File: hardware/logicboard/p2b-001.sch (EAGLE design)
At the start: 54 parts, among them IC1 74LS06N, IC2 4066N, J1 MKR, J2 GPIO, J3 Vcc, J4 RLY, J5 SPI, J7 DIN5, J8 DIN5, J9 DIN5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

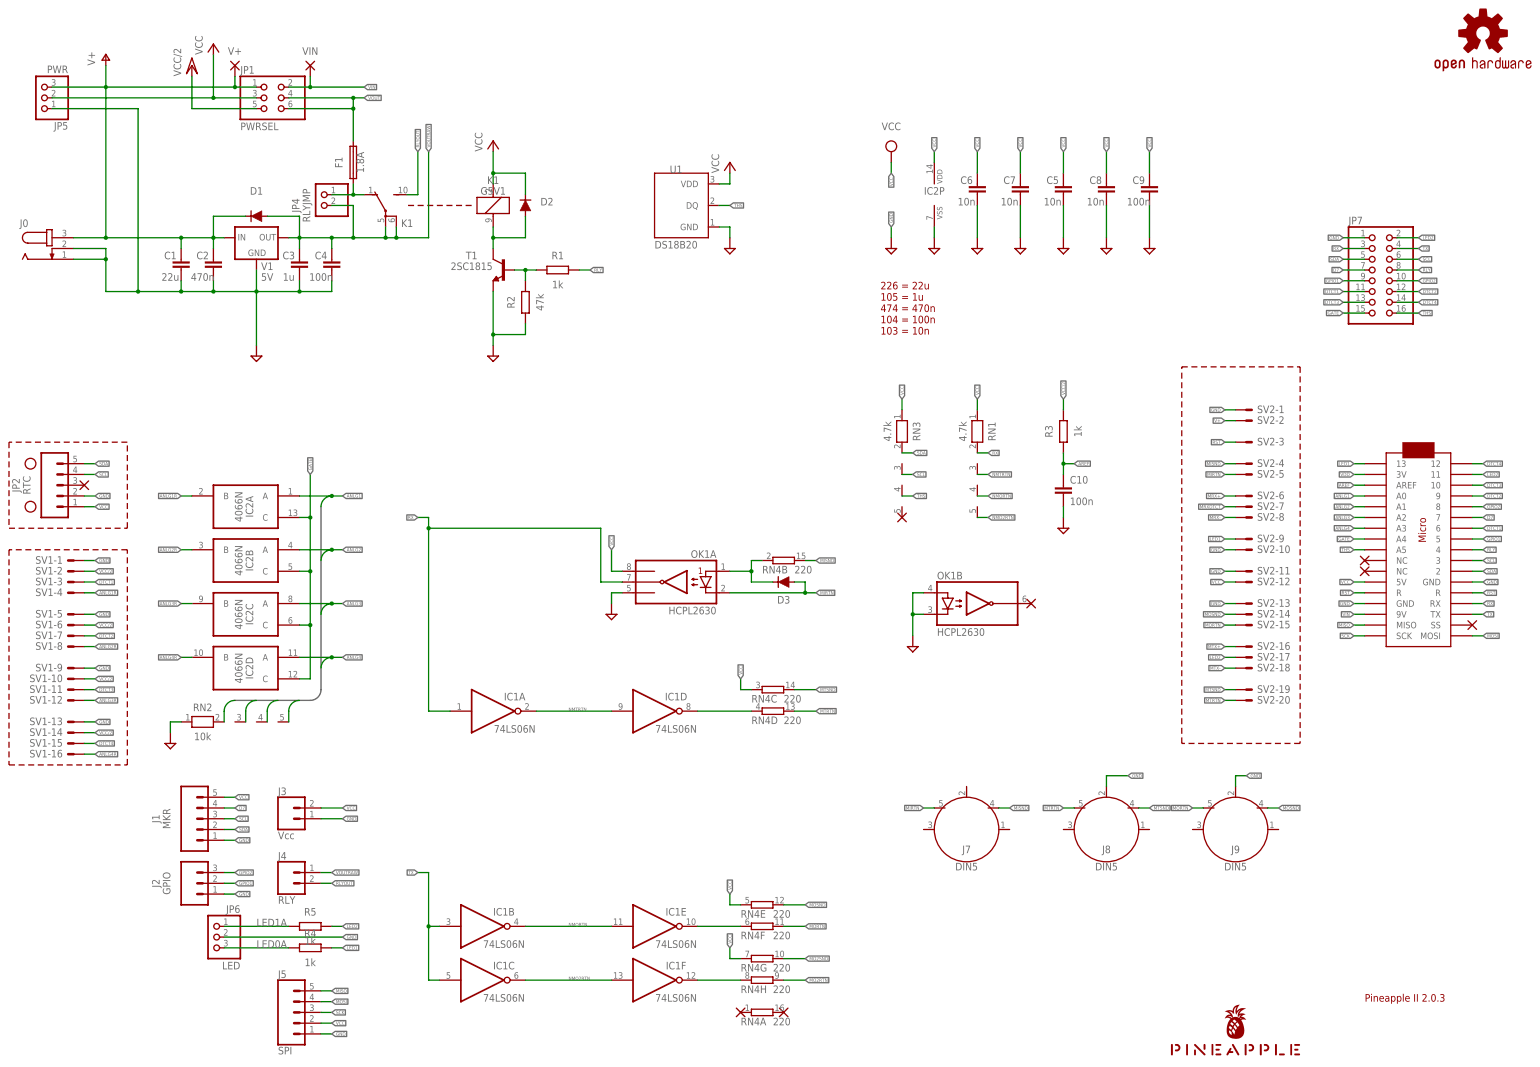
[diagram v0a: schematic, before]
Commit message: Followed Pineapple II 2.4.0 design. Before autorouting.
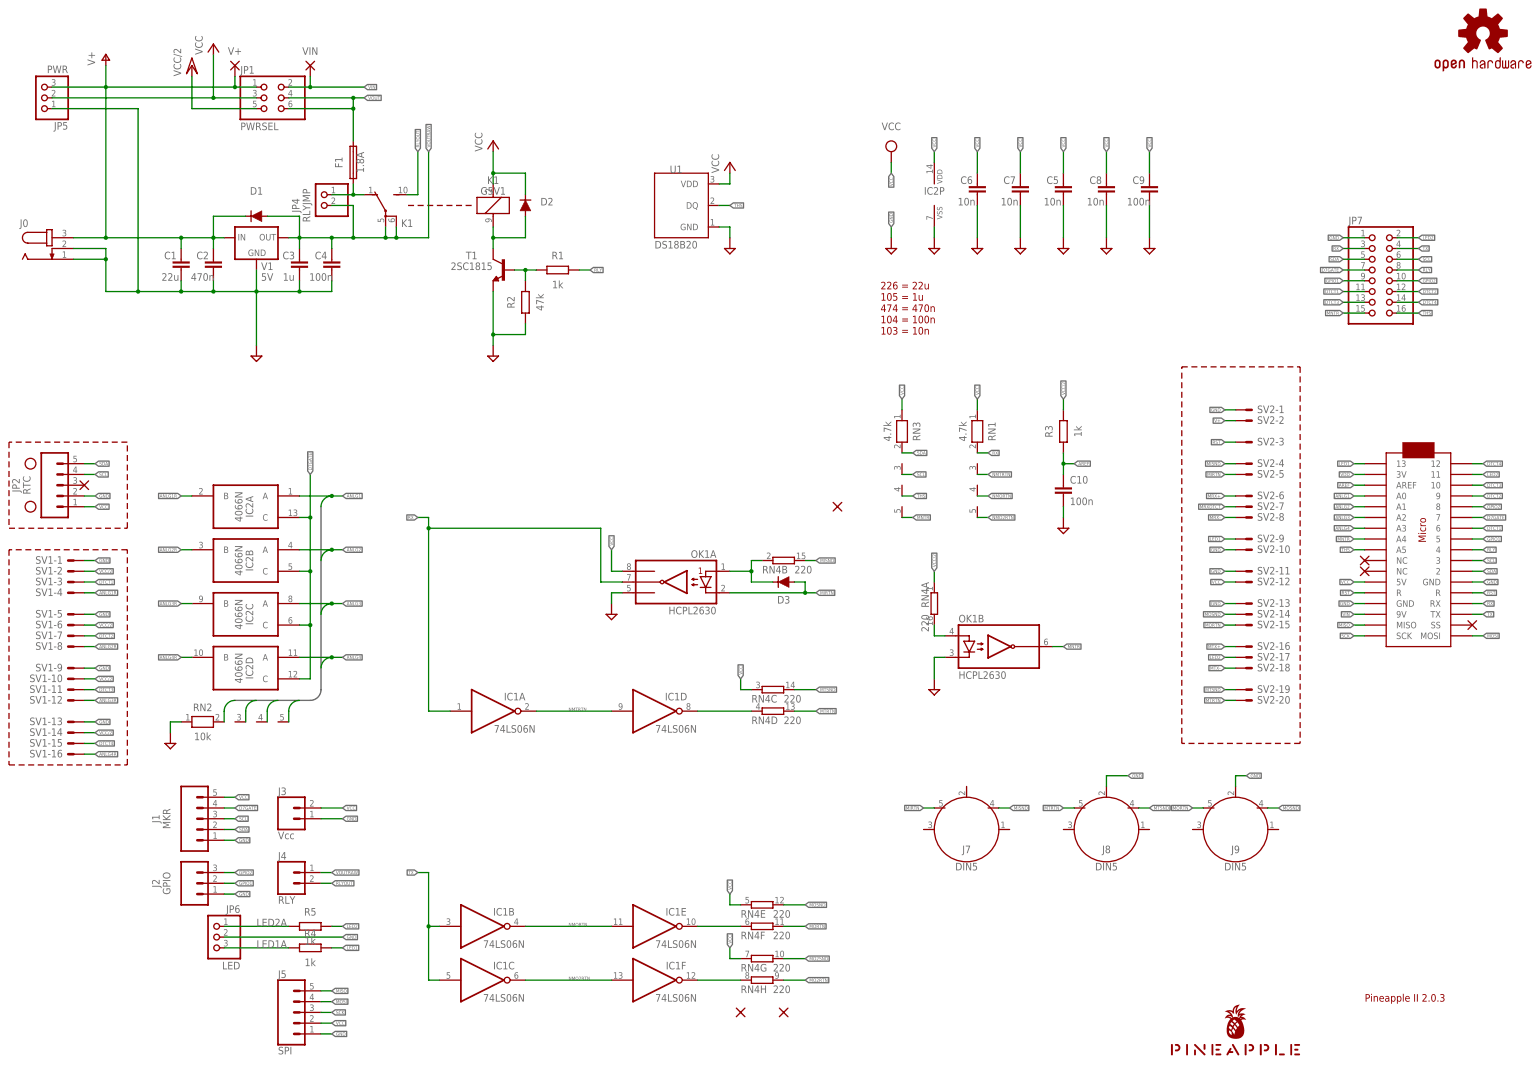
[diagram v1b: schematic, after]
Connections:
- removed net D7: J1.4, JP7.7, MC1.7
- removed net GATE: IC2A.C, IC2B.C, IC2C.C, IC2D.C, JP7.15, MC1.A4
- removed net LED0A: JP6.3, R4.1
- new net D7GATE: IC2A.C, IC2B.C, IC2C.C, IC2D.C, J1.4, JP7.7, MC1.7
- new net LED2A: JP6.1, R5.1
- new net MNTR: JP7.15, MC1.A4, OK1B.VO2, RN3.5
- new net MNTRA: OK1B.A2, RN4A.2
- net GND: no longer OK1B.A2
- net LED1A: now also JP6.3, R4.1; no longer JP6.1, R5.1
- net VCC/2: now also RN4A.1
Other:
- moved on the sheet: OK1B, RN4A
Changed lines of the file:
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@@
 <part name="OK1" library="optocoupler" library_urn="urn:adsk.eagle:library:320" deviceset="HCPL2630" device="" package3d_urn="urn:adsk.eagle:package:21941/1"/>
 <part name="SUPPLY1" library="supply2" deviceset="GND" device=""/>
-<part name="X2" library="wirepad" library_urn="urn:adsk.eagle:library:412" deviceset="PAD-N" device=""/>
 <part name="V+" library="wirepad" library_urn="urn:adsk.eagle:library:412" deviceset="SMD2" device="" package3d_urn="urn:adsk.eagle:package:30839/1"/>
 <part name="VIN" library="wirepad" library_urn="urn:adsk.eagle:library:412" deviceset="SMD2" device="" package3d_urn="urn:adsk.eagle:package:30839/1"/>
@@
 <attribute name="NAME" x="86.36" y="25.908" size="1.778" layer="95" font="vector"/>
 </instance>
-<instance part="RN4" gate="A" x="200.66" y="17.78" smashed="yes">
-<attribute name="VALUE" x="203.2" y="14.732" size="1.778" layer="96"/>
-<attribute name="NAME" x="195.58" y="14.732" size="1.778" layer="95"/>
+<instance part="RN4" gate="A" x="241.3" y="114.3" smashed="yes" rot="R270">
+<attribute name="VALUE" x="238.252" y="111.76" size="1.778" layer="96" rot="R270"/>
+<attribute name="NAME" x="238.252" y="119.38" size="1.778" layer="95" rot="R270"/>
 </instance>
 <instance part="RN4" gate="B" x="205.74" y="124.46" smashed="yes">
@@
 <attribute name="VALUE" x="231.14" y="154.94" size="1.778" layer="96" rot="R270" align="top-center"/>
 </instance>
-<instance part="X101" gate="G$1" x="233.68" y="134.62" smashed="yes"/>
+<instance part="X101" gate="G$1" x="218.44" y="137.16" smashed="yes"/>
 <instance part="OK1" gate="A" x="180.34" y="119.38" smashed="yes" rot="MR0">
 <attribute name="NAME" x="189.865" y="125.095" size="1.778" layer="95" rot="MR0"/>
 <attribute name="VALUE" x="189.865" y="111.76" size="1.778" layer="96" rot="MR0"/>
 </instance>
-<instance part="OK1" gate="B" x="251.46" y="114.3" smashed="yes">
-<attribute name="NAME" x="241.935" y="120.015" size="1.778" layer="95"/>
-<attribute name="VALUE" x="241.935" y="106.68" size="1.778" layer="96"/>
-</instance>
-<instance part="SUPPLY1" gate="GND" x="236.22" y="104.14" smashed="yes"/>
-<instance part="X2" gate="G$1" x="264.16" y="114.3" smashed="yes"/>
+<instance part="OK1" gate="B" x="256.54" y="104.14" smashed="yes">
+<attribute name="NAME" x="247.015" y="109.855" size="1.778" layer="95"/>
+<attribute name="VALUE" x="247.015" y="96.52" size="1.778" layer="96"/>
+</instance>
+<instance part="SUPPLY1" gate="GND" x="241.3" y="93.98" smashed="yes"/>
 <instance part="V+" gate="1" x="76.2" y="241.3" smashed="yes" rot="R270">
 <attribute name="NAME" x="76.2" y="243.84" size="1.778" layer="95" align="bottom-center"/>
@@
 </segment>
 <segment>
-<pinref part="OK1" gate="B" pin="A2"/>
-<wire x1="238.76" y1="116.84" x2="236.22" y2="116.84" width="0.1524" layer="91"/>
 <pinref part="OK1" gate="B" pin="C2"/>
-<wire x1="238.76" y1="111.76" x2="236.22" y2="111.76" width="0.1524" layer="91"/>
-<wire x1="236.22" y1="111.76" x2="236.22" y2="116.84" width="0.1524" layer="91"/>
-<wire x1="236.22" y1="111.76" x2="236.22" y2="106.68" width="0.1524" layer="91"/>
-<junction x="236.22" y="111.76"/>
+<wire x1="243.84" y1="101.6" x2="241.3" y2="101.6" width="0.1524" layer="91"/>
+<wire x1="241.3" y1="101.6" x2="241.3" y2="96.52" width="0.1524" layer="91"/>
 <pinref part="SUPPLY1" gate="GND" pin="GND"/>
 </segment>
@@
 </segment>
 </net>
-<net name="GATE" class="0">
+<net name="MNTR" class="0">
 <segment>
 <pinref part="MC1" gate="G$1" pin="A4"/>
 <wire x1="342.9" y1="129.54" x2="340.36" y2="129.54" width="0.1524" layer="91"/>
 <label x="340.36" y="129.54" size="0.8128" layer="95" rot="MR0" xref="yes"/>
+</segment>
+<segment>
+<pinref part="JP7" gate="A" pin="15"/>
+<wire x1="342.9" y1="182.88" x2="337.82" y2="182.88" width="0.1524" layer="91"/>
+<label x="337.82" y="182.88" size="0.8128" layer="95" rot="R180" xref="yes"/>
+</segment>
+<segment>
+<pinref part="RN3" gate="1" pin="5"/>
+<wire x1="233.68" y1="134.62" x2="236.22" y2="134.62" width="0.1524" layer="91"/>
+<label x="236.22" y="134.62" size="0.8128" layer="95" xref="yes"/>
+</segment>
+<segment>
+<pinref part="OK1" gate="B" pin="VO2"/>
+<wire x1="269.24" y1="104.14" x2="271.78" y2="104.14" width="0.1524" layer="91"/>
+<label x="271.78" y="104.14" size="0.8128" layer="95" xref="yes"/>
+</segment>
+</net>
+<net name="VDD" class="2">
+<segment>
+<pinref part="MC1" gate="G$1" pin="3V"/>
+<wire x1="342.9" y1="144.78" x2="340.36" y2="144.78" width="0.1524" layer="91"/>
+<label x="340.36" y="144.78" size="0.8128" layer="95" rot="MR0" xref="yes"/>
+</segment>
+</net>
+<net name="LED2" class="0">
+<segment>
+<pinref part="MC1" gate="G$1" pin="11"/>
+<wire x1="368.3" y1="144.78" x2="370.84" y2="144.78" width="0.1524" layer="91"/>
+<label x="370.84" y="144.78" size="0.8128" layer="95" xref="yes"/>
+</segment>
+<segment>
+<wire x1="99.06" y1="38.1" x2="101.6" y2="38.1" width="0.1524" layer="91"/>
+<label x="101.6" y="38.1" size="0.8128" layer="95" xref="yes"/>
+<pinref part="R5" gate="G$1" pin="2"/>
+</segment>
+<segment>
+<pinref part="JP7" gate="A" pin="2"/>
+<wire x1="350.52" y1="200.66" x2="355.6" y2="200.66" width="0.1524" layer="91"/>
+<label x="355.6" y="200.66" size="0.8128" layer="95" xref="yes"/>
+</segment>
+<segment>
+<pinref part="SV2" gate="-17" pin="S"/>
+<wire x1="312.42" y1="101.6" x2="309.88" y2="101.6" width="0.1524" layer="91"/>
+<label x="309.88" y="101.6" size="0.8128" layer="95" rot="MR0" xref="yes"/>
+</segment>
+</net>
+<net name="MRX-" class="0">
+<segment>
+<pinref part="SV2" gate="-8" pin="S"/>
+<wire x1="312.42" y1="134.62" x2="309.88" y2="134.62" width="0.1524" layer="91"/>
+<label x="309.88" y="134.62" size="0.8128" layer="95" rot="MR0" xref="yes"/>
+</segment>
+</net>
+<net name="D7GATE" class="0">
+<segment>
+<pinref part="MC1" gate="G$1" pin="7"/>
+<wire x1="368.3" y1="134.62" x2="370.84" y2="134.62" width="0.1524" layer="91"/>
+<label x="370.84" y="134.62" size="0.8128" layer="95" xref="yes"/>
+</segment>
+<segment>
+<pinref part="J1" gate="G$1" pin="4"/>
+<wire x1="73.66" y1="66.04" x2="76.2" y2="66.04" width="0.1524" layer="91"/>
+<label x="76.2" y="66.04" size="0.8128" layer="95" xref="yes"/>
+</segment>
+<segment>
+<pinref part="JP7" gate="A" pin="7"/>
+<wire x1="342.9" y1="193.04" x2="337.82" y2="193.04" width="0.1524" layer="91"/>
+<label x="337.82" y="193.04" size="0.8128" layer="95" rot="R180" xref="yes"/>
 </segment>
 <segment>
@@
 <label x="93.98" y="144.78" size="0.8128" layer="95" rot="R90" xref="yes"/>
 </segment>
-<segment>
-<pinref part="JP7" gate="A" pin="15"/>
-<wire x1="342.9" y1="182.88" x2="337.82" y2="182.88" width="0.1524" layer="91"/>
-<label x="337.82" y="182.88" size="0.8128" layer="95" rot="R180" xref="yes"/>
-</segment>
-</net>
-<net name="VDD" class="2">
-<segment>
-<pinref part="MC1" gate="G$1" pin="3V"/>
-<wire x1="342.9" y1="144.78" x2="340.36" y2="144.78" width="0.1524" layer="91"/>
-<label x="340.36" y="144.78" size="0.8128" layer="95" rot="MR0" xref="yes"/>
-</segment>
-</net>
-<net name="LED2" class="0">
-<segment>
-<pinref part="MC1" gate="G$1" pin="11"/>
-<wire x1="368.3" y1="144.78" x2="370.84" y2="144.78" width="0.1524" layer="91"/>
-<label x="370.84" y="144.78" size="0.8128" layer="95" xref="yes"/>
-</segment>
-<segment>
-<wire x1="99.06" y1="38.1" x2="101.6" y2="38.1" width="0.1524" layer="91"/>
-<label x="101.6" y="38.1" size="0.8128" layer="95" xref="yes"/>
-<pinref part="R5" gate="G$1" pin="2"/>
-</segment>
-<segment>
-<pinref part="JP7" gate="A" pin="2"/>
-<wire x1="350.52" y1="200.66" x2="355.6" y2="200.66" width="0.1524" layer="91"/>
-<label x="355.6" y="200.66" size="0.8128" layer="95" xref="yes"/>
-</segment>
-<segment>
-<pinref part="SV2" gate="-17" pin="S"/>
-<wire x1="312.42" y1="101.6" x2="309.88" y2="101.6" width="0.1524" layer="91"/>
-<label x="309.88" y="101.6" size="0.8128" layer="95" rot="MR0" xref="yes"/>
-</segment>
-</net>
-<net name="MRX-" class="0">
-<segment>
-<pinref part="SV2" gate="-8" pin="S"/>
-<wire x1="312.42" y1="134.62" x2="309.88" y2="134.62" width="0.1524" layer="91"/>
-<label x="309.88" y="134.62" size="0.8128" layer="95" rot="MR0" xref="yes"/>
-</segment>
-</net>
-<net name="D7" class="0">
-<segment>
-<pinref part="MC1" gate="G$1" pin="7"/>
-<wire x1="368.3" y1="134.62" x2="370.84" y2="134.62" width="0.1524" layer="91"/>
-<label x="370.84" y="134.62" size="0.8128" layer="95" xref="yes"/>
-</segment>
-<segment>
-<pinref part="J1" gate="G$1" pin="4"/>
-<wire x1="73.66" y1="66.04" x2="76.2" y2="66.04" width="0.1524" layer="91"/>
-<label x="76.2" y="66.04" size="0.8128" layer="95" xref="yes"/>
-</segment>
-<segment>
-<pinref part="JP7" gate="A" pin="7"/>
-<wire x1="342.9" y1="193.04" x2="337.82" y2="193.04" width="0.1524" layer="91"/>
-<label x="337.82" y="193.04" size="0.8128" layer="95" rot="R180" xref="yes"/>
-</segment>
 </net>
 <net name="GPIO2" class="0">
@@
 <wire x1="81.28" y1="231.14" x2="66.04" y2="231.14" width="0.1524" layer="91"/>
 </segment>
-</net>
-<net name="LED1A" class="0">
+<segment>
+<pinref part="RN4" gate="A" pin="1"/>
+<wire x1="241.3" y1="119.38" x2="241.3" y2="121.92" width="0.1524" layer="91"/>
+<label x="241.3" y="121.92" size="0.8128" layer="95" rot="R90" xref="yes"/>
+</segment>
+</net>
+<net name="LED2A" class="0">
 <segment>
 <wire x1="88.9" y1="38.1" x2="73.66" y2="38.1" width="0.1524" layer="91"/>
@@
 </segment>
 </net>
-<net name="LED0A" class="0">
+<net name="LED1A" class="0">
 <segment>
 <wire x1="88.9" y1="33.02" x2="73.66" y2="33.02" width="0.1524" layer="91"/>
@@
 </segment>
 </net>
+<net name="MNTRA" class="0">
+<segment>
+<pinref part="OK1" gate="B" pin="A2"/>
+<wire x1="243.84" y1="106.68" x2="241.3" y2="106.68" width="0.1524" layer="91"/>
+<pinref part="RN4" gate="A" pin="2"/>
+<wire x1="241.3" y1="106.68" x2="241.3" y2="109.22" width="0.1524" layer="91"/>
+</segment>
+</net>
